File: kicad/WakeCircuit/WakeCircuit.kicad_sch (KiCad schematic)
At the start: 11 parts, among them U1 TLV7011DBVR, U2 CD4013BE

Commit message: PCB updates
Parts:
- added C3: 100nF, symbol Device:C
- added C4: 10uF, symbol Device:C_Polarized
- added J1: Conn_01x12_Socket, Connector_PinSocket_2.54mm:PinSocket_1x12_P2.54mm_Vertical, symbol Connector:Conn_01x12_Socket
- added J2: Conn_01x10_Socket, Connector_PinSocket_2.54mm:PinSocket_1x10_P2.54mm_Vertical, symbol Connector:Conn_01x10_Socket
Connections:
- net +3V3: now also U2.9 (D2), C3.1, C4.1
- net GND: now also C3.2, C4.2; no longer U2.9 (D2)
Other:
- moved on the sheet: C1, C2, D1, LDR1, R1, R2, R3, R4, RV1, U1, U2

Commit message: PCB Update
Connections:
- net +3V3: now also J2.1 (Pin_1)
- net ESP32 GPIO 5 Wake: now also J1.3 (Pin_3)
- net GND: now also J1.1 (Pin_1), J1.9 (Pin_9), J2.10 (Pin_10), J2.6 (Pin_6)
- no-connect marks 2 -> 18
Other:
- moved on the sheet: C1, C2, C3, C4, D1, J2, LDR1, R1, R2, R3, R4, RV1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

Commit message: Cleanup schematic
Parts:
- removed U2: CD4013BE, N14, symbol CD4013:CD4013BE
- added U3: 4013, symbol 4xxx:4013
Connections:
- net +3V3: now also U3.14 (VDD), U3.5 (D), U3.9 (D)
- net ESP32 GPIO 5 Wake: now also U3.13 (Q)
- net GND: now also U3.6 (S), U3.7 (VSS), U3.8 (S)
- net at D1.1 (K), R4.2: now also U3.1 (Q)
- net at C1.1, R4.1: now also U3.10 (R)
- net at R3.1, U1.1 (OUT): now also U3.11 (C), U3.3 (C)
- net at C2.1, D1.2 (A), R2.1: now also U3.4 (R)
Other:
- moved on the sheet: C1, C2, C3, C4, D1, J2, LDR1, R1, R2, R3, R4, RV1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

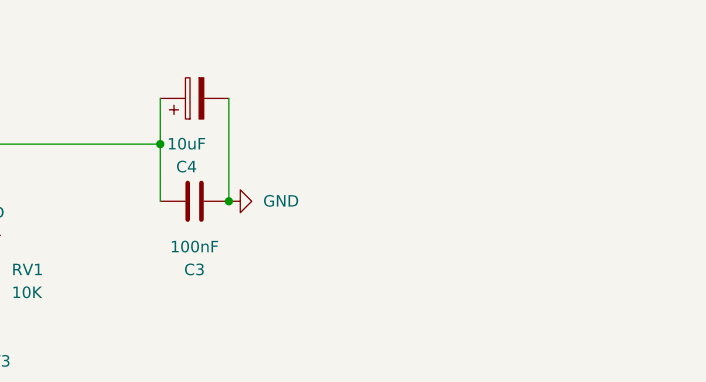
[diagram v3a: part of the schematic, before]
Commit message: Assigned footprints
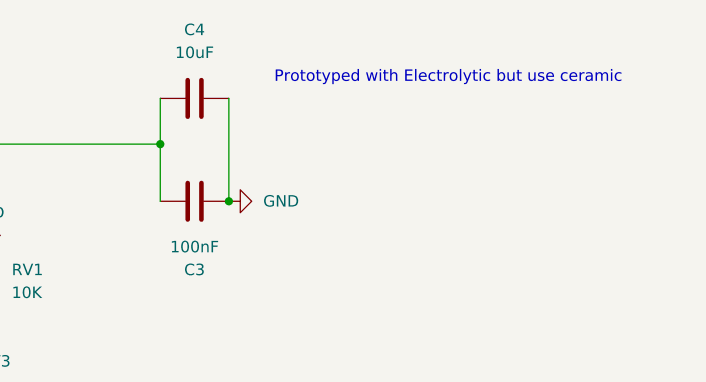
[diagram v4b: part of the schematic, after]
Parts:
- removed C4: 10uF, symbol Device:C_Polarized
- added C4: 10uF, Capacitor_SMD:C_0805_2012Metric, symbol Device:C
- C1, C3: footprint (none) -> Capacitor_SMD:C_0805_2012Metric
- C2: footprint (none) -> Capacitor_Tantalum_SMD:CP_EIA-3216-18_Kemet-A
- R1: footprint Resistor_THT:R_Axial_DIN0207_L6.3mm_D2.5mm_P5.08mm_Vertical -> Resistor_SMD:R_0805_2012Metric
- R2, R3, R4: footprint (none) -> Resistor_SMD:R_0805_2012Metric
- U3: footprint (none) -> Package_SO:TSSOP-14_4.4x5mm_P0.65mm
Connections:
- net +3V3: now also C4.2
- net GND: now also C4.1
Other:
- note added: "Prototyped with Electrolytic but use ceramic"
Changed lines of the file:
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@@
 		)
 	)
+	(text "Prototyped with Electrolytic but use ceramic"
+		(exclude_from_sim no)
+		(at 258.064 24.384 0)
+		(effects
+			(font
+				(size 1.27 1.27)
+			)
+		)
+	)
 	(text_box "Flip Flop 1 Starts a 30 second lockout timer that prevents flip flop 2 from waking the esp32 unless no activity has been seen on the light diode for more than 30 seconds\n"
 		(exclude_from_sim no)
@@
 			)
 		)
+		(property "Sim.Device" "R"
+			(at 207.01 46.99 0)
+			(effects
+				(font
+					(size 1.27 1.27)
+				)
+				(hide yes)
+			)
+		)
+		(property "Sim.Type" "POT"
+			(at 207.01 46.99 0)
+			(effects
+				(font
+					(size 1.27 1.27)
+				)
+				(hide yes)
+			)
+		)
+		(property "Sim.Pins" "1=r0 2=wiper 3=r1"
+			(at 207.01 46.99 0)
+			(effects
+				(font
+					(size 1.27 1.27)
+				)
+				(hide yes)
+			)
+		)
+		(property "Sim.Params" "r=\"\""
+			(at 207.01 46.99 0)
+			(effects
+				(font
+					(size 1.27 1.27)
+				)
+				(hide yes)
+			)
+		)
 		(pin "1"
 		)
@@
 			)
 		)
-		(property "Footprint" ""
+		(property "Footprint" "Resistor_SMD:R_0805_2012Metric"
 			(at 123.19 92.202 90)
 			(effects
@@
 			)
 		)
-		(property "Footprint" ""
+		(property "Footprint" "Capacitor_Tantalum_SMD:CP_EIA-3216-18_Kemet-A"
 			(at 134.62 93.0148 0)
 			(effects
@@
 			)
 		)
-		(property "Footprint" ""
+		(property "Footprint" "Capacitor_SMD:C_0805_2012Metric"
 			(at 233.68 37.1348 0)
 			(effects
@@
 			)
 		)
-		(property "Footprint" ""
+		(property "Footprint" "Resistor_SMD:R_0805_2012Metric"
 			(at 163.83 103.632 90)
 			(effects
@@
 	)
 	(symbol
+		(lib_id "Device:C")
+		(at 229.87 26.67 270)
+		(unit 1)
+		(exclude_from_sim no)
+		(in_bom yes)
+		(on_board yes)
+		(dnp no)
+		(fields_autoplaced yes)
+		(property "Reference" "C4"
+			(at 229.87 19.05 90)
+			(effects
+				(font
+					(size 1.27 1.27)
+				)
+			)
+		)
+		(property "Value" "10uF"
+			(at 229.87 21.59 90)
+			(effects
+				(font
+					(size 1.27 1.27)
+				)
+			)
+		)
+		(property "Footprint" "Capacitor_SMD:C_0805_2012Metric"
+			(at 226.06 27.6352 0)
+			(effects
+				(font
+					(size 1.27 1.27)
+				)
+				(hide yes)
+			)
+		)
+		(property "Datasheet" "~"
+			(at 229.87 26.67 0)
+			(effects
+				(font
+					(size 1.27 1.27)
+				)
+				(hide yes)
+			)
+		)
+		(property "Description" "Unpolarized capacitor"
+			(at 229.87 26.67 0)
+			(effects
+				(font
+					(size 1.27 1.27)
+				)
+				(hide yes)
+			)
+		)
+		(pin "1"
+		)
+		(pin "2"
+		)
+		(instances
+			(project ""
+				(path "/37cf770b-fa56-49dc-98af-b2d65e07667b"
+					(reference "C4")
+					(unit 1)
+				)
+			)
+		)
+	)
+	(symbol
 		(lib_id "power:+3V3")
 		(at 191.77 36.83 270)
@@
 			)
 		)
-		(property "Footprint" "Resistor_THT:R_Axial_DIN0207_L6.3mm_D2.5mm_P5.08mm_Vertical"
+		(property "Footprint" "Resistor_SMD:R_0805_2012Metric"
 			(at 152.908 50.8 90)
 			(effects
@@
 			)
 		)
-		(property "Footprint" ""
+		(property "Footprint" "Resistor_SMD:R_0805_2012Metric"
 			(at 118.11 56.642 90)
 			(effects
@@
 			)
 		)
-		(property "Footprint" ""
+		(property "Footprint" "Capacitor_SMD:C_0805_2012Metric"
 			(at 177.8 104.4448 0)
 			(effects
@@
 	)
 	(symbol
-		(lib_id "Device:C_Polarized")
-		(at 229.87 26.67 90)
-		(unit 1)
-		(exclude_from_sim no)
-		(in_bom yes)
-		(on_board yes)
-		(dnp no)
-		(fields_autoplaced yes)
-		(property "Reference" "C4"
-			(at 228.981 34.29 90)
-			(effects
-				(font
-					(size 1.27 1.27)
-				)
-			)
-		)
-		(property "Value" "10uF"
-			(at 228.981 31.75 90)
-			(effects
-				(font
-					(size 1.27 1.27)
-				)
-			)
-		)
-		(property "Footprint" ""
-			(at 233.68 25.7048 0)
-			(effects
-				(font
-					(size 1.27 1.27)
-				)
-				(hide yes)
-			)
-		)
-		(property "Datasheet" "~"
-			(at 229.87 26.67 0)
-			(effects
-				(font
-					(size 1.27 1.27)
-				)
-				(hide yes)
-			)
-		)
-		(property "Description" "Polarized capacitor"
-			(at 229.87 26.67 0)
-			(effects
-				(font
-					(size 1.27 1.27)
-				)
-				(hide yes)
-			)
-		)
-		(pin "2"
-		)
-		(pin "1"
-		)
-		(instances
-			(project ""
-				(path "/37cf770b-fa56-49dc-98af-b2d65e07667b"
-					(reference "C4")
-					(unit 1)
-				)
-			)
-		)
-	)
-	(symbol
 		(lib_id "4xxx:4013")
 		(at 165.1 82.55 180)
@@
 			)
 		)
-		(property "Footprint" ""
+		(property "Footprint" "Package_SO:TSSOP-14_4.4x5mm_P0.65mm"
 			(at 165.1 82.55 0)
 			(effects
@@
 			)
 		)
-		(property "Footprint" ""
+		(property "Footprint" "Package_SO:TSSOP-14_4.4x5mm_P0.65mm"
 			(at 259.08 91.44 0)
 			(effects
@@
 			)
 		)
-		(property "Footprint" ""
+		(property "Footprint" "Package_SO:TSSOP-14_4.4x5mm_P0.65mm"
 			(at 207.01 100.33 0)
 			(effects

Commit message: PCB layout
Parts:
- added J4: Conn_01x03_Socket, Connector_JST:JST_PH_S3B-PH-K_1x03_P2.00mm_Horizontal, symbol Connector:Conn_01x03_Socket
- added LDR2: GL5539, OptoDevice:R_LDR_4.9x4.2mm_P2.54mm_Vertical, symbol Sensor_Optical:VT93xx
- added R5: 1.2K, Resistor_SMD:R_0805_2012Metric, symbol Device:R
- D1: footprint Diode_THT:D_DO-35_SOD27_P7.62mm_Horizontal -> Diode_SMD:D_SOD-123F
- RV1: footprint Potentiometer_THT:Potentiometer_Bourns_3386W_Horizontal -> Potentiometer_SMD:Potentiometer_Bourns_3214J_Horizontal
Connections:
- net +3V3: now also J4.3 (Pin_3); no longer LDR1.2
- net GND: now also R5.2
- net LDR_SIG: now reaches R1.2, U1.3 (IN+)
- net LDR_SIG: now also J4.1 (Pin_1); no longer LDR1.1
- net GPIO_1: now reaches J1.11 (Pin_11)
- net GPIO_1: now also J4.2 (Pin_2), R5.1
- net ESP32 GPIO 5 Wake renamed GPIO_5
- no-connect marks 18 -> 21
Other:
- note added: "External LDRs plug in here"
- note added: "Wake GPIO Pin"
- title: (none) -> M5Stamp C3 shield to wake on light detected
- moved on the sheet: R1, R3, RV1, U1

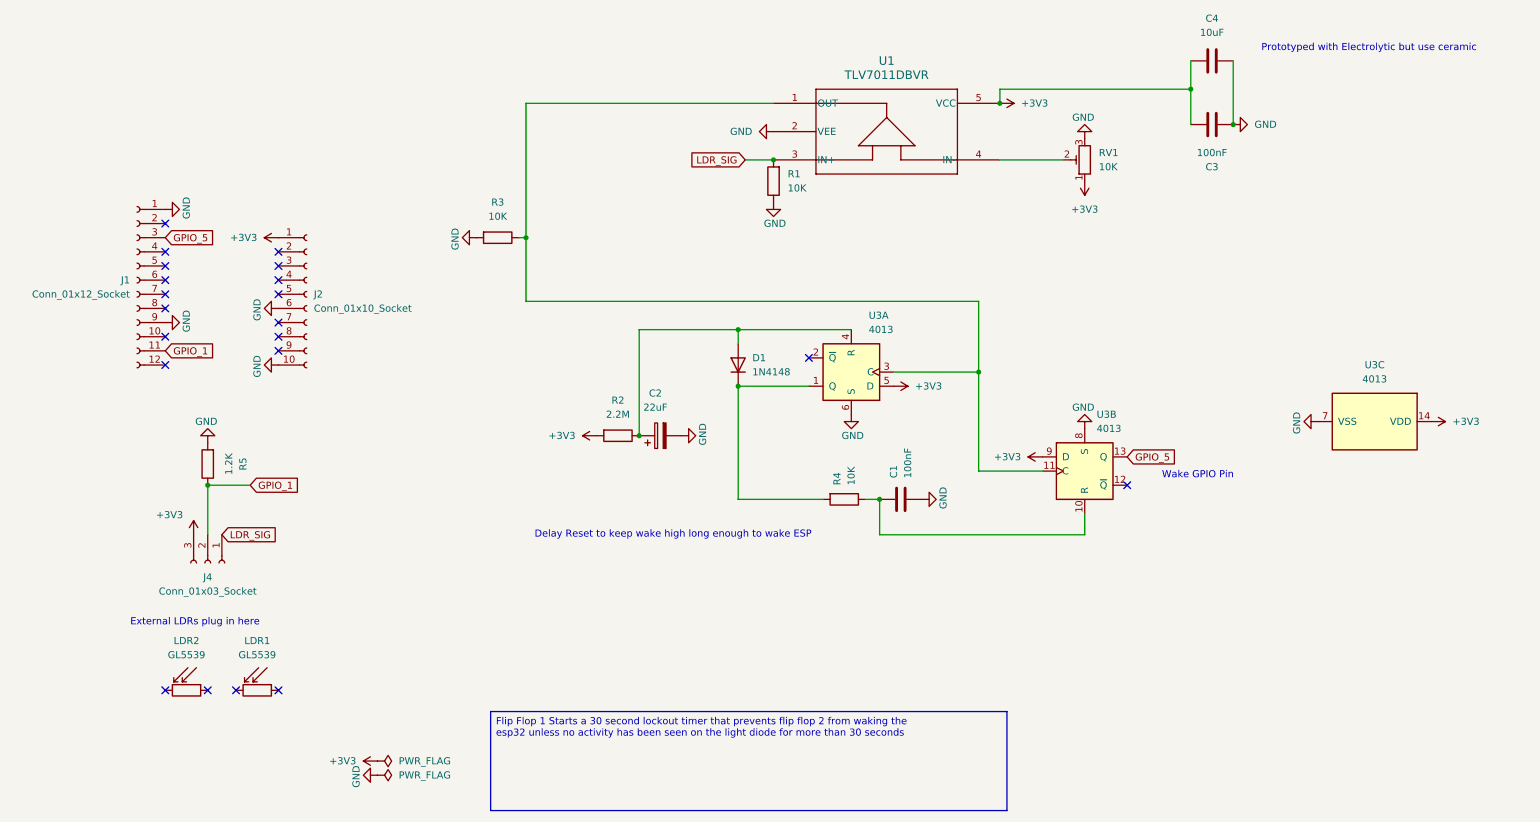
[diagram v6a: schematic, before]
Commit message: Update BOM with Part Numbers
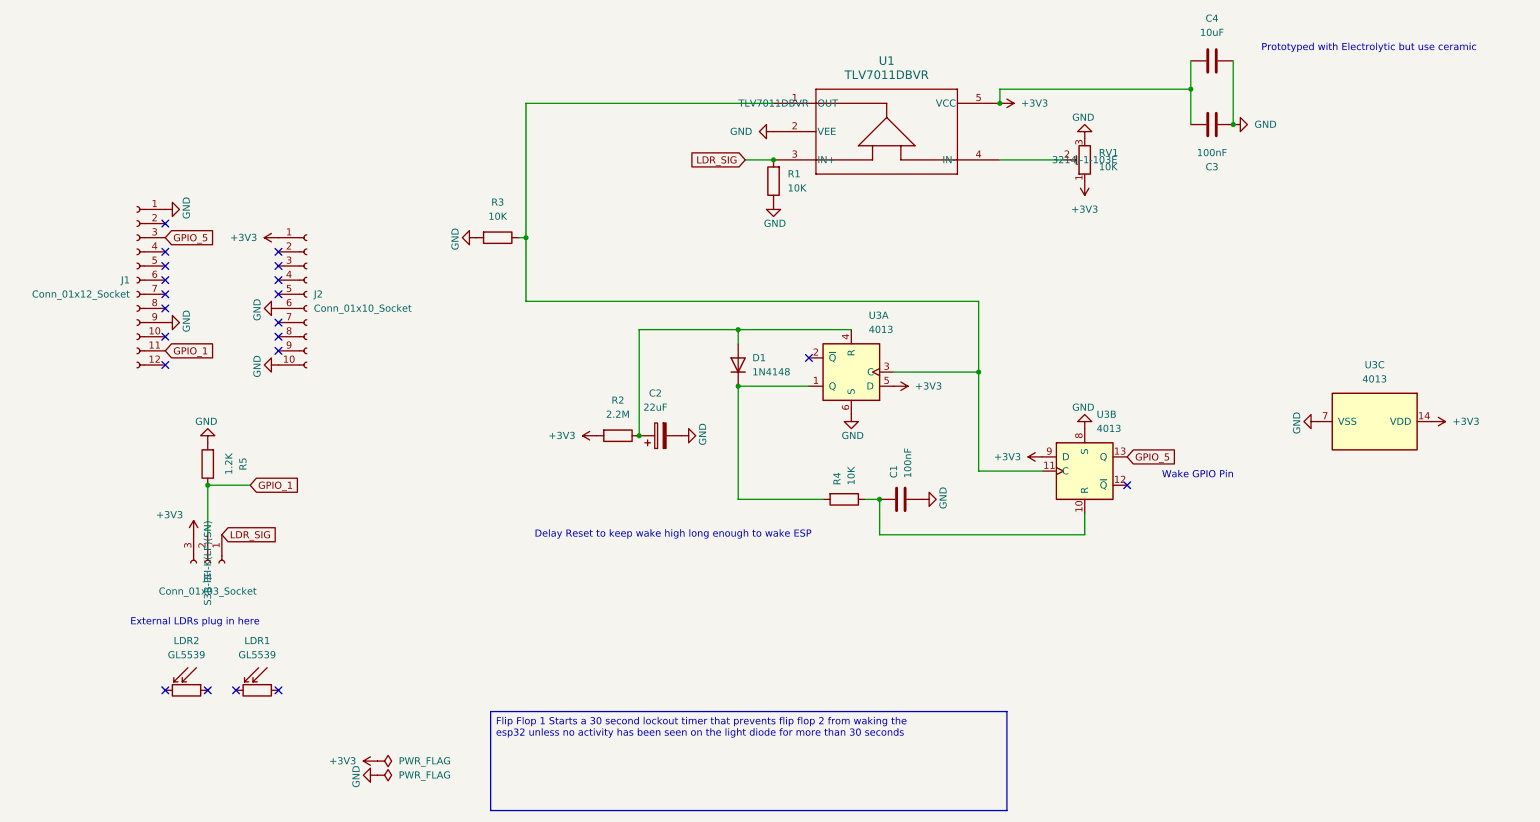
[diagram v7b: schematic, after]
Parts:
- C1, C3: PartNumber (none) -> CC0805KKX7R0BB104
- C2: PartNumber (none) -> TAJA226K010RNJ
- C4: PartNumber (none) -> CL21A106MPFNNNE
- D1: PartNumber (none) -> 1N4148W-7-F
- J1: PartNumber (none) -> BCS-112-L-S-TE
- J2: PartNumber (none) -> BCS-110-L-S-TE
- J4: PartNumber (none) -> S3B-PH-K(LF)(SN)
- LDR1, LDR2: now left out of the parts list
- R1, R3, R4: PartNumber (none) -> RC0805FR-0710KL
- R2: PartNumber (none) -> RC0805FR-072M2L
- R5: PartNumber (none) -> RC0805FR-071K2L
- RV1: PartNumber (none) -> 3214J-1-103E
- U1: PartNumber (none) -> TLV7011DBVR
- U3: PartNumber (none) -> CD4013BPW
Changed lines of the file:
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@@
 			)
 		)
+		(property "PartNumber" "3214J-1-103E"
+			(at 207.01 44.45 0)
+			(effects
+				(font
+					(size 1.27 1.27)
+				)
+			)
+		)
 		(pin "1"
 		)
@@
 			)
 		)
+		(property "PartNumber" "S3B-PH-K(LF)(SN)"
+			(at 49.53 116.84 0)
+			(effects
+				(font
+					(size 1.27 1.27)
+				)
+			)
+		)
 		(pin "3"
 		)
@@
 			)
 		)
+		(property "PartNumber" "TLV7011DBVR"
+			(at 151.13 34.29 0)
+			(effects
+				(font
+					(size 1.27 1.27)
+				)
+			)
+		)
 		(pin "2"
 		)
@@
 			)
 		)
+		(property "PartNumber" "1N4148W-7-F "
+			(at 144.78 81.28 90)
+			(effects
+				(font
+					(size 1.27 1.27)
+				)
+				(hide yes)
+			)
+		)
 		(pin "1"
 		)
@@
 			)
 		)
+		(property "PartNumber" "RC0805FR-072M2L "
+			(at 123.19 93.98 90)
+			(effects
+				(font
+					(size 1.27 1.27)
+				)
+				(hide yes)
+			)
+		)
 		(pin "1"
 		)
@@
 			)
 		)
+		(property "PartNumber" "BCS-112-L-S-TE"
+			(at 36.83 66.04 0)
+			(effects
+				(font
+					(size 1.27 1.27)
+				)
+				(hide yes)
+			)
+		)
 		(pin "7"
 		)
@@
 			)
 		)
+		(property "PartNumber" "TAJA226K010RNJ "
+			(at 130.81 93.98 90)
+			(effects
+				(font
+					(size 1.27 1.27)
+				)
+				(hide yes)
+			)
+		)
 		(pin "2"
 		)
@@
 		(unit 1)
 		(exclude_from_sim no)
-		(in_bom yes)
+		(in_bom no)
 		(on_board no)
 		(dnp no)
@@
 			)
 		)
+		(property "PartNumber" "BCS-110-L-S-TE"
+			(at 67.31 68.58 0)
+			(effects
+				(font
+					(size 1.27 1.27)
+				)
+				(hide yes)
+			)
+		)
 		(pin "6"
 		)
@@
 			)
 		)
+		(property "PartNumber" "CC0805KKX7R0BB104 "
+			(at 229.87 38.1 90)
+			(effects
+				(font
+					(size 1.27 1.27)
+				)
+				(hide yes)
+			)
+		)
 		(pin "2"
 		)
@@
 			)
 		)
+		(property "PartNumber" "RC0805FR-0710KL "
+			(at 163.83 105.41 0)
+			(effects
+				(font
+					(size 1.27 1.27)
+				)
+				(hide yes)
+			)
+		)
 		(pin "1"
 		)
@@
 			)
 		)
+		(property "PartNumber" "CL21A106MPFNNNE"
+			(at 229.87 26.67 90)
+			(effects
+				(font
+					(size 1.27 1.27)
+				)
+				(hide yes)
+			)
+		)
 		(pin "1"
 		)
@@
 			)
 		)
+		(property "PartNumber" "RC0805FR-0710KL "
+			(at 151.13 48.26 0)
+			(effects
+				(font
+					(size 1.27 1.27)
+				)
+				(hide yes)
+			)
+		)
 		(pin "1"
 		)
@@
 			)
 		)
+		(property "PartNumber" "RC0805FR-0710KL "
+			(at 101.6 58.42 90)
+			(effects
+				(font
+					(size 1.27 1.27)
+				)
+				(hide yes)
+			)
+		)
 		(pin "1"
 		)
@@
 			)
 		)
+		(property "PartNumber" "CC0805KKX7R0BB104 "
+			(at 173.99 105.41 0)
+			(effects
+				(font
+					(size 1.27 1.27)
+				)
+				(hide yes)
+			)
+		)
 		(pin "2"
 		)
@@
 			)
 		)
+		(property "PartNumber" "RC0805FR-071K2L"
+			(at 49.53 99.06 90)
+			(effects
+				(font
+					(size 1.27 1.27)
+				)
+				(hide yes)
+			)
+		)
 		(pin "1"
 		)
@@
 			)
 		)
+		(property "PartNumber" "CD4013BPW "
+			(at 165.1 82.55 0)
+			(effects
+				(font
+					(size 1.27 1.27)
+				)
+				(hide yes)
+			)
+		)
 		(pin "3"
 		)
@@
 			)
 		)
+		(property "PartNumber" "CD4013BPW "
+			(at 259.08 91.44 0)
+			(effects
+				(font
+					(size 1.27 1.27)
+				)
+				(hide yes)
+			)
+		)
 		(pin "3"
 		)
@@
 		(unit 1)
 		(exclude_from_sim no)
-		(in_bom yes)
+		(in_bom no)
 		(on_board no)
 		(dnp no)
@@
 			(at 207.01 100.33 0)
 			(effects
+				(font
+					(size 1.27 1.27)
+				)
+				(hide yes)
+			)
+		)
+		(property "PartNumber" "CD4013BPW "
+			(at 207.01 100.33 0)
+			(effects
